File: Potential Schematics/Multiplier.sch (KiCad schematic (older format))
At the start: 11 parts

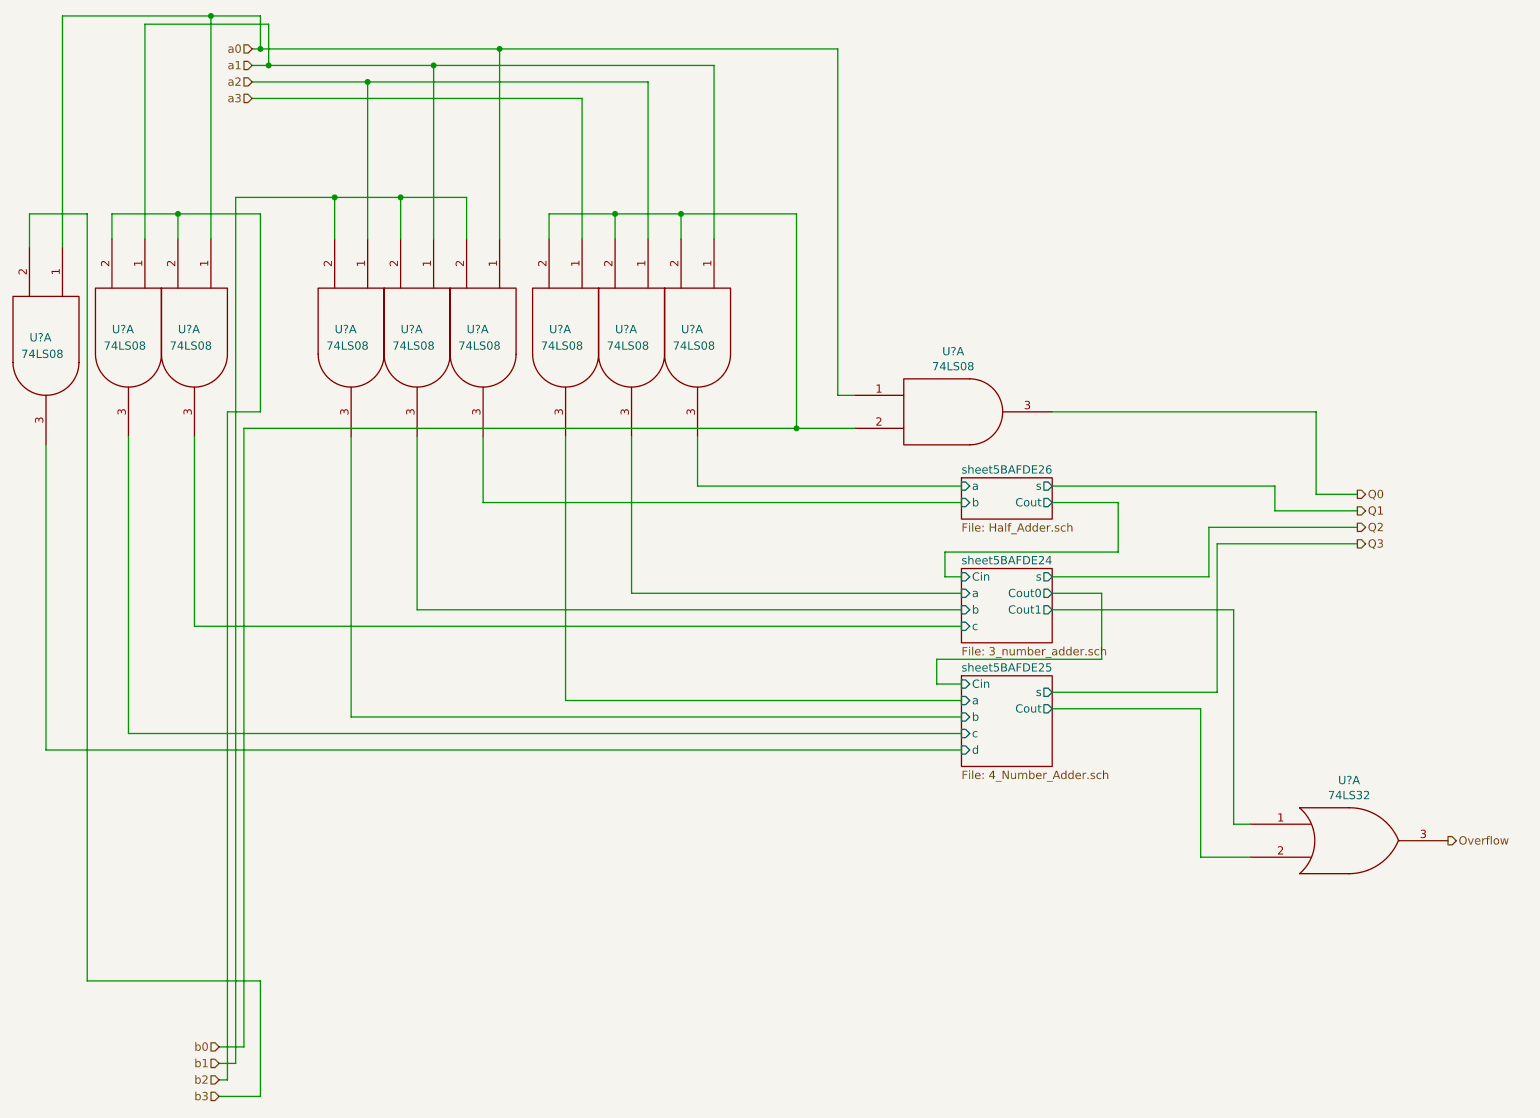
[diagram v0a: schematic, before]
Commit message: Updated overview of Schematic
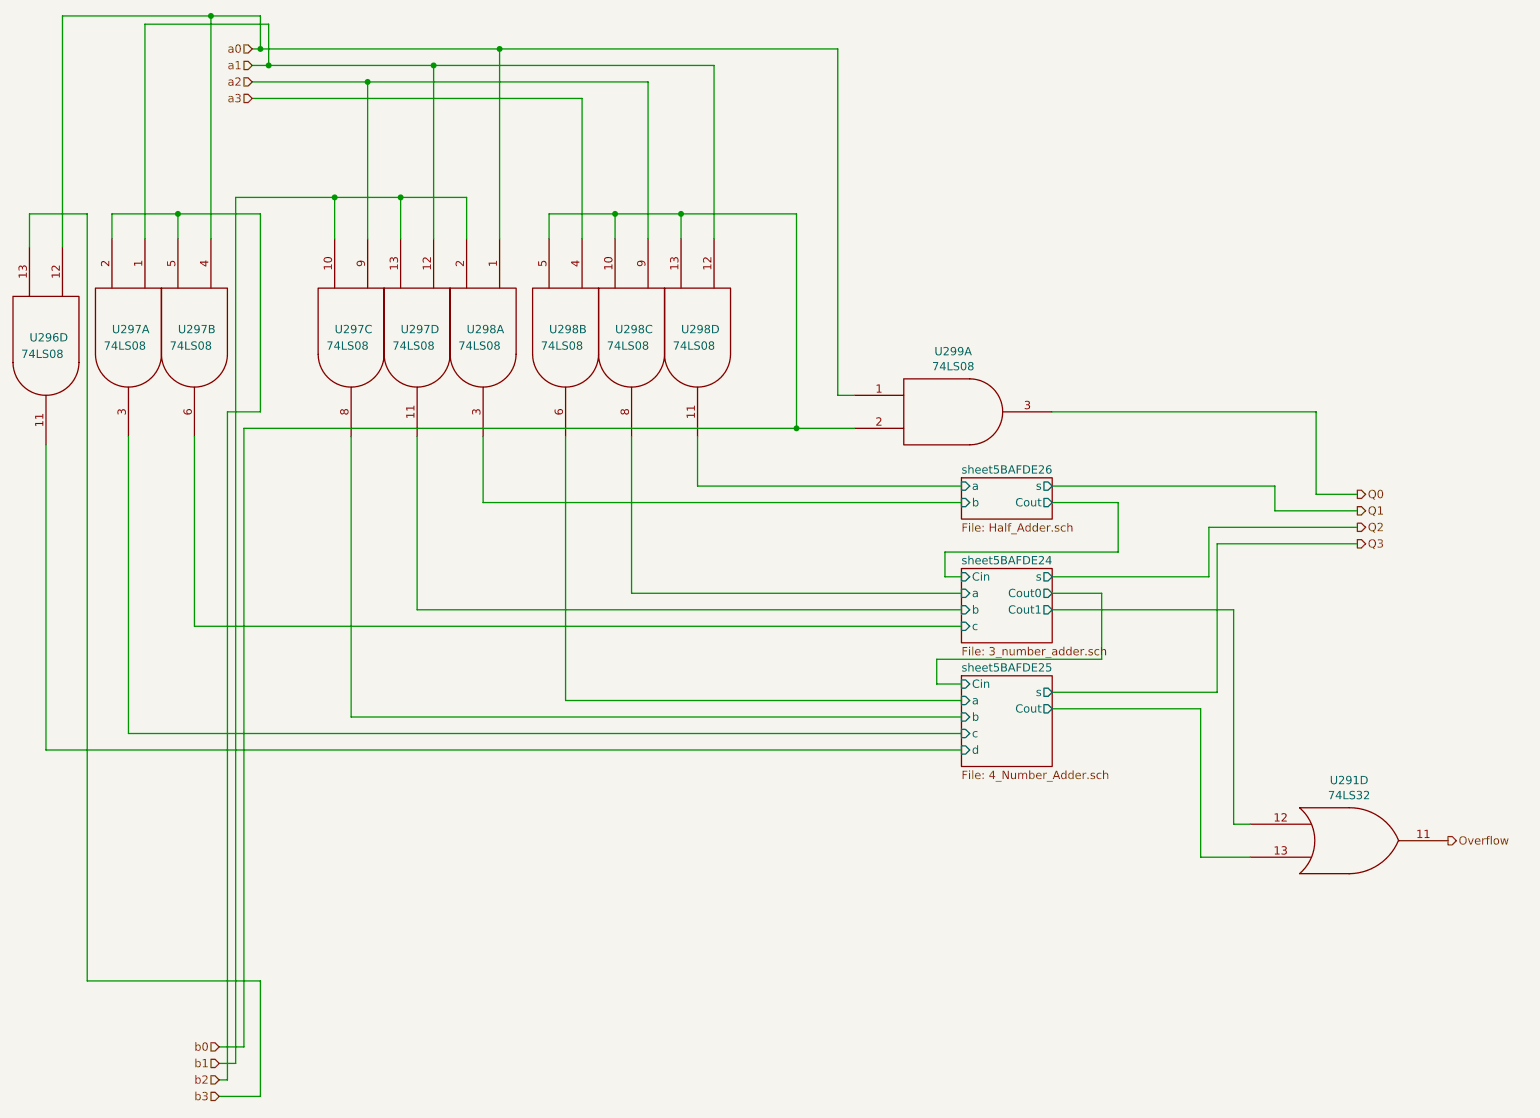
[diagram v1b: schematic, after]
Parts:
- gave numbers to parts that had none: 5
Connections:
- net Overflow: now also U291.11; no longer U291.3
- net a0: now also U296.12, U297.4; no longer U296.1, U297.1
- net a1: now also U297.12, U298.12; no longer U297.1, U298.1
- net a2: now also U297.9, U298.9; no longer U297.1, U298.1
- net a3: now also U298.4; no longer U298.1
- net b0: now also U298.10, U298.13, U298.5; no longer U298.2, U298.2, U298.2
- net b1: now also U297.10, U297.13; no longer U297.2, U297.2
- net b2: now also U297.5; no longer U297.2
- net b3: now also U296.13; no longer U296.2
- net sheet5BAFDE24/Cout1: now also U291.12; no longer U291.1
- net sheet5BAFDE24/a: now also U298.8; no longer U298.3
- net sheet5BAFDE24/b: now also U297.11; no longer U297.3
- net sheet5BAFDE24/c: now also U297.6; no longer U297.3
- net sheet5BAFDE25/Cout: now also U291.13; no longer U291.2
- net sheet5BAFDE25/a: now also U298.6; no longer U298.3
- net sheet5BAFDE25/b: now also U297.8; no longer U297.3
- net sheet5BAFDE25/d: now also U296.11; no longer U296.3
- net sheet5BAFDE26/a: now also U298.11; no longer U298.3
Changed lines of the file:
@@
 $Descr A4 11693 8268
 encoding utf-8
-Sheet 452 467
+Sheet 452 902
 Title ""
 Date ""
@@
 $Comp
 L 4-bit_processor-rescue:74LS32 U?
-U 1 1 5BAFDE57
+U 4 1 5BAFDE57
 P 8950 5750
 AR Path="/5B9D167A/5BAA33A0/5BAFDE57" Ref="U?"  Part="1"
-AR Path="/5B9D167A/5BAA33A0/5BAFDB78/5BAFDE57" Ref="U?"  Part="1"
-F 0 "U?" H 8950 6116 50  0000 C CNN
+AR Path="/5B9D167A/5BAA33A0/5BAFDB78/5BAFDE57" Ref="U291"  Part="4"
+F 0 "U291" H 8950 6116 50  0000 C CNN
 F 1 "74LS32" H 8950 6025 50  0000 C CNN
 F 2 "" H 8950 5750 50  0001 C CNN
 F 3 "" H 8950 5750 50  0001 C CNN
-	1    8950 5750
+	4    8950 5750
 	1    0    0    -1
 $EndComp
@@
 P 6550 3150
 AR Path="/5B9D167A/5BAA33A0/5BAFDE6C" Ref="U?"  Part="1"
-AR Path="/5B9D167A/5BAA33A0/5BAFDB78/5BAFDE6C" Ref="U?"  Part="1"
-F 0 "U?" H 6550 3516 50  0000 C CNN
+AR Path="/5B9D167A/5BAA33A0/5BAFDB78/5BAFDE6C" Ref="U299"  Part="1"
+F 0 "U299" H 6550 3516 50  0000 C CNN
 F 1 "74LS08" H 6550 3425 50  0000 C CNN
 F 2 "" H 6550 3150 50  0001 C CNN
@@
 $Comp
 L 4-bit_processor-rescue:74LS08 U?
-U 1 1 5BAFDE79
+U 4 1 5BAFDE79
 P 5000 2700
 AR Path="/5B9D167A/5BAA33A0/5BAFDE79" Ref="U?"  Part="1"
-AR Path="/5B9D167A/5BAA33A0/5BAFDB78/5BAFDE79" Ref="U?"  Part="1"
-F 0 "U?" V 4950 2600 50  0000 L CNN
+AR Path="/5B9D167A/5BAA33A0/5BAFDB78/5BAFDE79" Ref="U298"  Part="4"
+F 0 "U298" V 4950 2600 50  0000 L CNN
 F 1 "74LS08" V 5050 2550 50  0000 L CNN
 F 2 "" H 5000 2700 50  0001 C CNN
 F 3 "" H 5000 2700 50  0001 C CNN
-	1    5000 2700
+	4    5000 2700
 	0    1    1    0
 $EndComp
@@
 $Comp
 L 4-bit_processor-rescue:74LS08 U?
-U 1 1 5BAFDE8C
+U 3 1 5BAFDE8C
 P 4600 2700
 AR Path="/5B9D167A/5BAA33A0/5BAFDE8C" Ref="U?"  Part="1"
-AR Path="/5B9D167A/5BAA33A0/5BAFDB78/5BAFDE8C" Ref="U?"  Part="1"
-F 0 "U?" V 4550 2600 50  0000 L CNN
+AR Path="/5B9D167A/5BAA33A0/5BAFDB78/5BAFDE8C" Ref="U298"  Part="3"
+F 0 "U298" V 4550 2600 50  0000 L CNN
 F 1 "74LS08" V 4650 2550 50  0000 L CNN
 F 2 "" H 4600 2700 50  0001 C CNN
 F 3 "" H 4600 2700 50  0001 C CNN
-	1    4600 2700
-	0    1    1    0
-$EndComp
-$Comp
-L 4-bit_processor-rescue:74LS08 U?
-U 1 1 5BAFDE93
+	3    4600 2700
+	0    1    1    0
+$EndComp
+$Comp
+L 4-bit_processor-rescue:74LS08 U?
+U 2 1 5BAFDE93
 P 4200 2700
 AR Path="/5B9D167A/5BAA33A0/5BAFDE93" Ref="U?"  Part="1"
-AR Path="/5B9D167A/5BAA33A0/5BAFDB78/5BAFDE93" Ref="U?"  Part="1"
-F 0 "U?" V 4150 2600 50  0000 L CNN
+AR Path="/5B9D167A/5BAA33A0/5BAFDB78/5BAFDE93" Ref="U298"  Part="2"
+F 0 "U298" V 4150 2600 50  0000 L CNN
 F 1 "74LS08" V 4250 2550 50  0000 L CNN
 F 2 "" H 4200 2700 50  0001 C CNN
 F 3 "" H 4200 2700 50  0001 C CNN
-	1    4200 2700
+	2    4200 2700
 	0    1    1    0
 $EndComp
@@
 P 3700 2700
 AR Path="/5B9D167A/5BAA33A0/5BAFDEA8" Ref="U?"  Part="1"
-AR Path="/5B9D167A/5BAA33A0/5BAFDB78/5BAFDEA8" Ref="U?"  Part="1"
-F 0 "U?" V 3650 2600 50  0000 L CNN
+AR Path="/5B9D167A/5BAA33A0/5BAFDB78/5BAFDEA8" Ref="U298"  Part="1"
+F 0 "U298" V 3650 2600 50  0000 L CNN
 F 1 "74LS08" V 3750 2550 50  0000 L CNN
 F 2 "" H 3700 2700 50  0001 C CNN
@@
 $Comp
 L 4-bit_processor-rescue:74LS08 U?
-U 1 1 5BAFDEAF
+U 4 1 5BAFDEAF
 P 3300 2700
 AR Path="/5B9D167A/5BAA33A0/5BAFDEAF" Ref="U?"  Part="1"
-AR Path="/5B9D167A/5BAA33A0/5BAFDB78/5BAFDEAF" Ref="U?"  Part="1"
-F 0 "U?" V 3250 2600 50  0000 L CNN
+AR Path="/5B9D167A/5BAA33A0/5BAFDB78/5BAFDEAF" Ref="U297"  Part="4"
+F 0 "U297" V 3250 2600 50  0000 L CNN
 F 1 "74LS08" V 3350 2550 50  0000 L CNN
 F 2 "" H 3300 2700 50  0001 C CNN
 F 3 "" H 3300 2700 50  0001 C CNN
-	1    3300 2700
-	0    1    1    0
-$EndComp
-$Comp
-L 4-bit_processor-rescue:74LS08 U?
-U 1 1 5BAFDEB6
+	4    3300 2700
+	0    1    1    0
+$EndComp
+$Comp
+L 4-bit_processor-rescue:74LS08 U?
+U 3 1 5BAFDEB6
 P 2900 2700
 AR Path="/5B9D167A/5BAA33A0/5BAFDEB6" Ref="U?"  Part="1"
-AR Path="/5B9D167A/5BAA33A0/5BAFDB78/5BAFDEB6" Ref="U?"  Part="1"
-F 0 "U?" V 2850 2600 50  0000 L CNN
+AR Path="/5B9D167A/5BAA33A0/5BAFDB78/5BAFDEB6" Ref="U297"  Part="3"
+F 0 "U297" V 2850 2600 50  0000 L CNN
 F 1 "74LS08" V 2950 2550 50  0000 L CNN
 F 2 "" H 2900 2700 50  0001 C CNN
 F 3 "" H 2900 2700 50  0001 C CNN
-	1    2900 2700
+	3    2900 2700
 	0    1    1    0
 $EndComp
@@
 $Comp
 L 4-bit_processor-rescue:74LS08 U?
-U 1 1 5BAFDED6
+U 2 1 5BAFDED6
 P 1950 2700
 AR Path="/5B9D167A/5BAA33A0/5BAFDED6" Ref="U?"  Part="1"
-AR Path="/5B9D167A/5BAA33A0/5BAFDB78/5BAFDED6" Ref="U?"  Part="1"
-F 0 "U?" V 1900 2600 50  0000 L CNN
+AR Path="/5B9D167A/5BAA33A0/5BAFDB78/5BAFDED6" Ref="U297"  Part="2"
+F 0 "U297" V 1900 2600 50  0000 L CNN
 F 1 "74LS08" V 2000 2550 50  0000 L CNN
 F 2 "" H 1950 2700 50  0001 C CNN
 F 3 "" H 1950 2700 50  0001 C CNN
-	1    1950 2700
+	2    1950 2700
 	0    1    1    0
 $EndComp
@@
 P 1550 2700
 AR Path="/5B9D167A/5BAA33A0/5BAFDEDD" Ref="U?"  Part="1"
-AR Path="/5B9D167A/5BAA33A0/5BAFDB78/5BAFDEDD" Ref="U?"  Part="1"
-F 0 "U?" V 1500 2600 50  0000 L CNN
+AR Path="/5B9D167A/5BAA33A0/5BAFDB78/5BAFDEDD" Ref="U297"  Part="1"
+F 0 "U297" V 1500 2600 50  0000 L CNN
 F 1 "74LS08" V 1600 2550 50  0000 L CNN
 F 2 "" H 1550 2700 50  0001 C CNN
@@
 $Comp
 L 4-bit_processor-rescue:74LS08 U?
-U 1 1 5BAFDEE4
+U 4 1 5BAFDEE4
 P 1050 2750
 AR Path="/5B9D167A/5BAA33A0/5BAFDEE4" Ref="U?"  Part="1"
-AR Path="/5B9D167A/5BAA33A0/5BAFDB78/5BAFDEE4" Ref="U?"  Part="1"
-F 0 "U?" V 1000 2650 50  0000 L CNN
+AR Path="/5B9D167A/5BAA33A0/5BAFDB78/5BAFDEE4" Ref="U296"  Part="4"
+F 0 "U296" V 1000 2650 50  0000 L CNN
 F 1 "74LS08" V 1100 2600 50  0000 L CNN
 F 2 "" H 1050 2750 50  0001 C CNN
 F 3 "" H 1050 2750 50  0001 C CNN
-	1    1050 2750
-	0    1    1    0
-$EndComp
+	4    1050 2750
+	0    1    1    0
+$EndComp
